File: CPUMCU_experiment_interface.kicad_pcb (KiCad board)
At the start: 2 copper layers, 2 parts, among them J1 LCD Connector, U1 6581SID

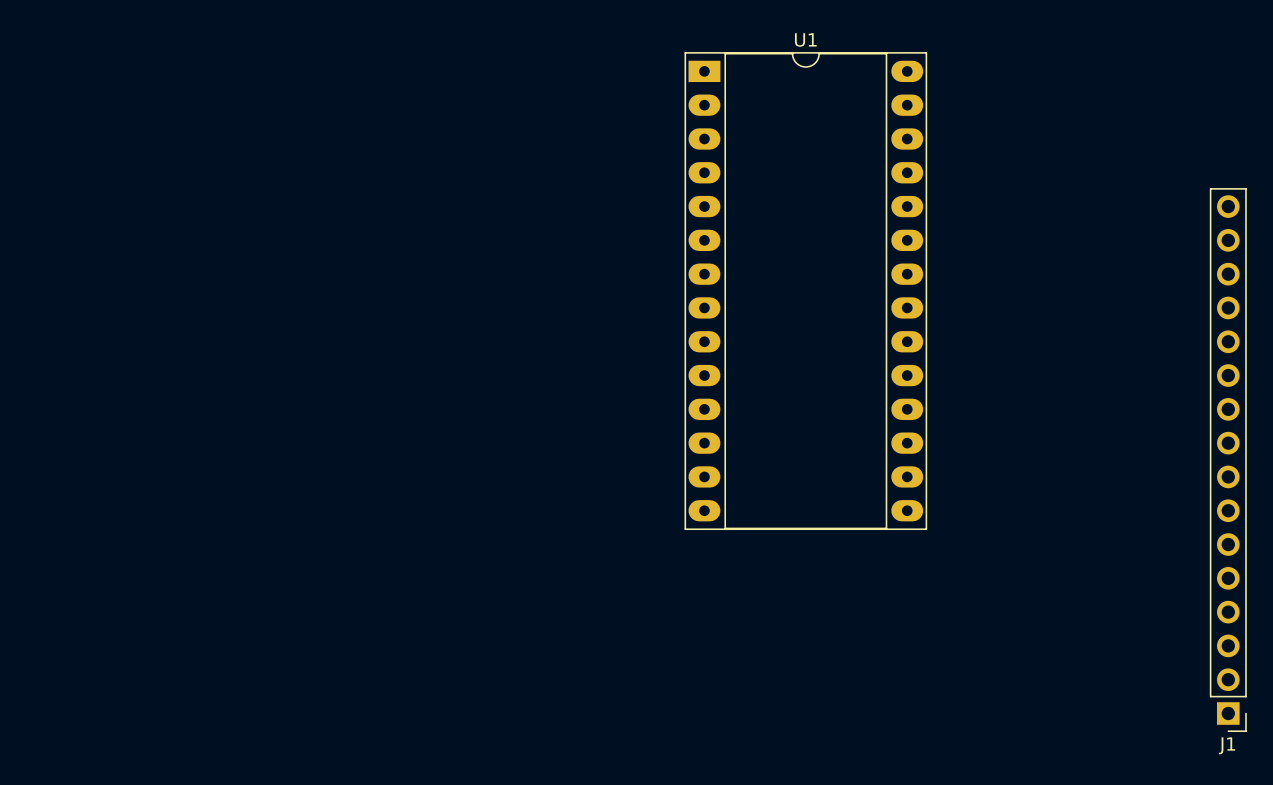
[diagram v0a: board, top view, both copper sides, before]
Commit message: Added EPROM and temporary microSD card reader
microSD card reader will probably be replaced.
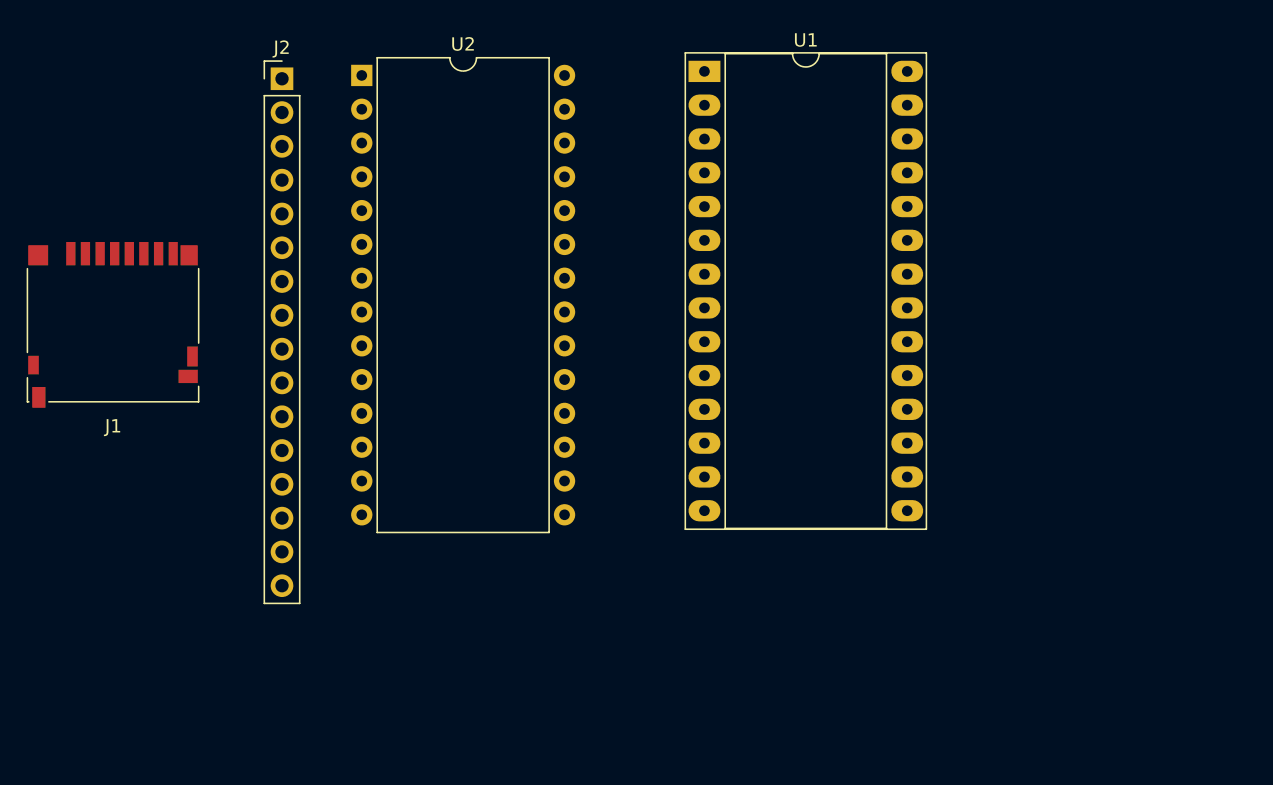
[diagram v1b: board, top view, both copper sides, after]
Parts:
- added J2: LCD Connector, Connector_PinHeader_2.54mm:PinHeader_1x16_P2.54mm_Vertical, F.Cu at (134.6, 88.2)
- added U2: 27C256, Package_DIP:DIP-28_W15.24mm, F.Cu at (140.6, 87.9)
- J1: value LCD Connector -> Micro_SD_Card_Det_Hirose_DM3AT; footprint Connector_PinHeader_2.54mm:PinHeader_1x16_P2.54mm_Vertical -> microSD:microSD_HC_Hirose_DM3D-SF
- moved J1 88.8 mm to (121.9, 106.7)
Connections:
- net Net-(U1-Pad5) renamed /~SID_RES
- net Net-(U1-Pad6) renamed /SID_CLK
- net Net-(U1-Pad8) renamed /~SID_CS
- J1 pad 1: GND -> Net-(J1-Pad1)
- J1 pad 10: /D3 -> Net-(J1-Pad10)
- J1 pad 11: /D4 -> Net-(J1-Pad11)
- J1 pad 2: +5V -> Net-(J1-Pad2)
- J1 pad 5: /R~W -> Net-(J1-Pad5)
- J1 pad 7: /D0 -> Net-(J1-Pad7)
- J1 pad 8: /D1 -> Net-(J1-Pad8)
- J1 pad 9: /D2 -> Net-(J1-Pad9)
